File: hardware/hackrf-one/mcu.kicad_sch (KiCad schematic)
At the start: 131 parts, among them J1 USB-MICRO-B, P20 GPIO, P22 I2S, P23 DBGEN, P24 TRST, P25 LPC_ISP, P26 LPC_JTAG, P28 SD, P29 CPLD_JTAG, P3 GND, P30 BANK2_AUX, P5 LEDS, P68 SPIFI_CS, P69 VREGMODE, P70 EN_1V8, P71 ID, P73 P1_2, P74 P1_1, P75 GP_CLKIN, P76 GP_CLKIN, P77 GP_CLKIN, P78 GP_CLKIN, P79 GP_CLKIN, P80 SHIELD, P81 SPIFI_SIO2, P82 SPIFI_SIO3, Q5 MOSFET_P, SW1 DFU, SW2 RESET, U15 TVS, U20 W25Q80, U21 TPS62410, U23 LPC4320FBD144, U24 GSG-XC2C64A-7VQG100C, X2 MCU_XTAL, X3 RTC_XTAL

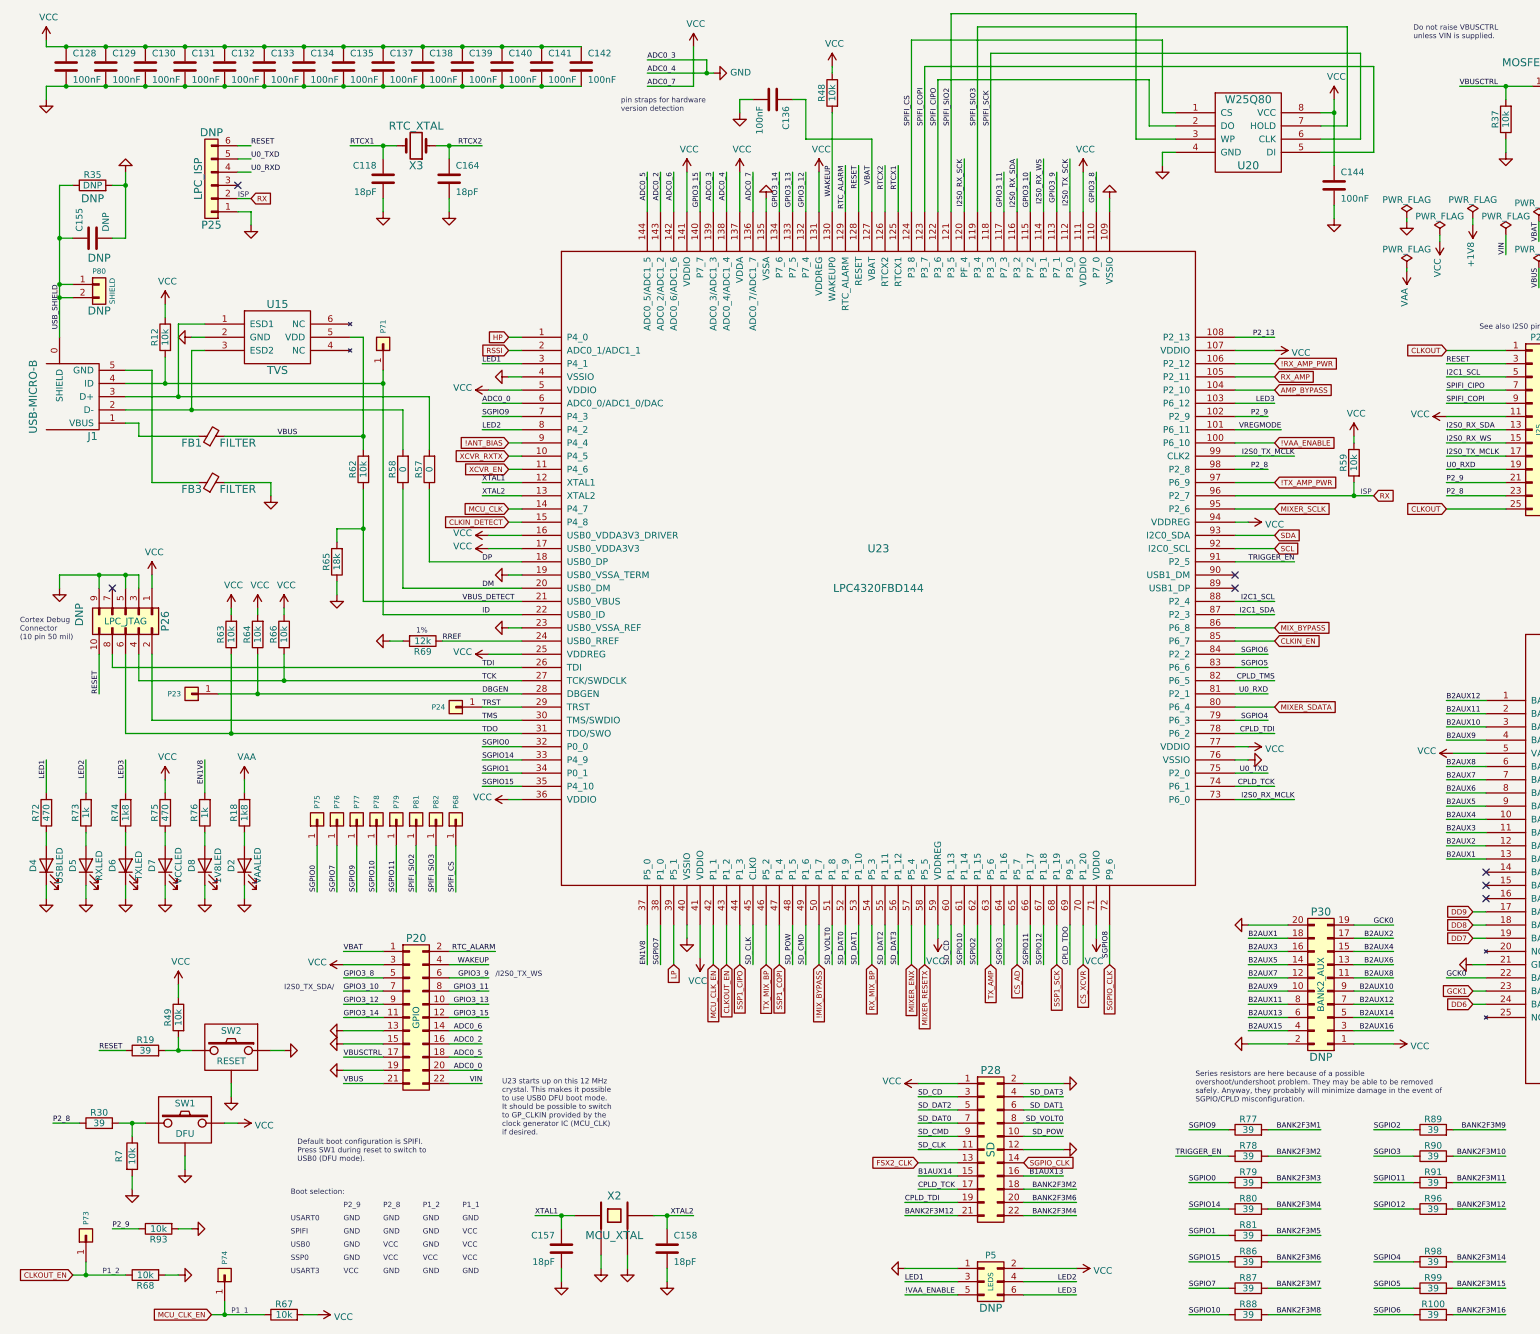
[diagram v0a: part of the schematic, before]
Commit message: HackRF One: revert hardware design to 8727449
This commit is between r8 and r9 and will be used as the basis for r10.
It includes some of the changes in r9 but predates the major changes to
the clock generator and IF transceiver ICs.
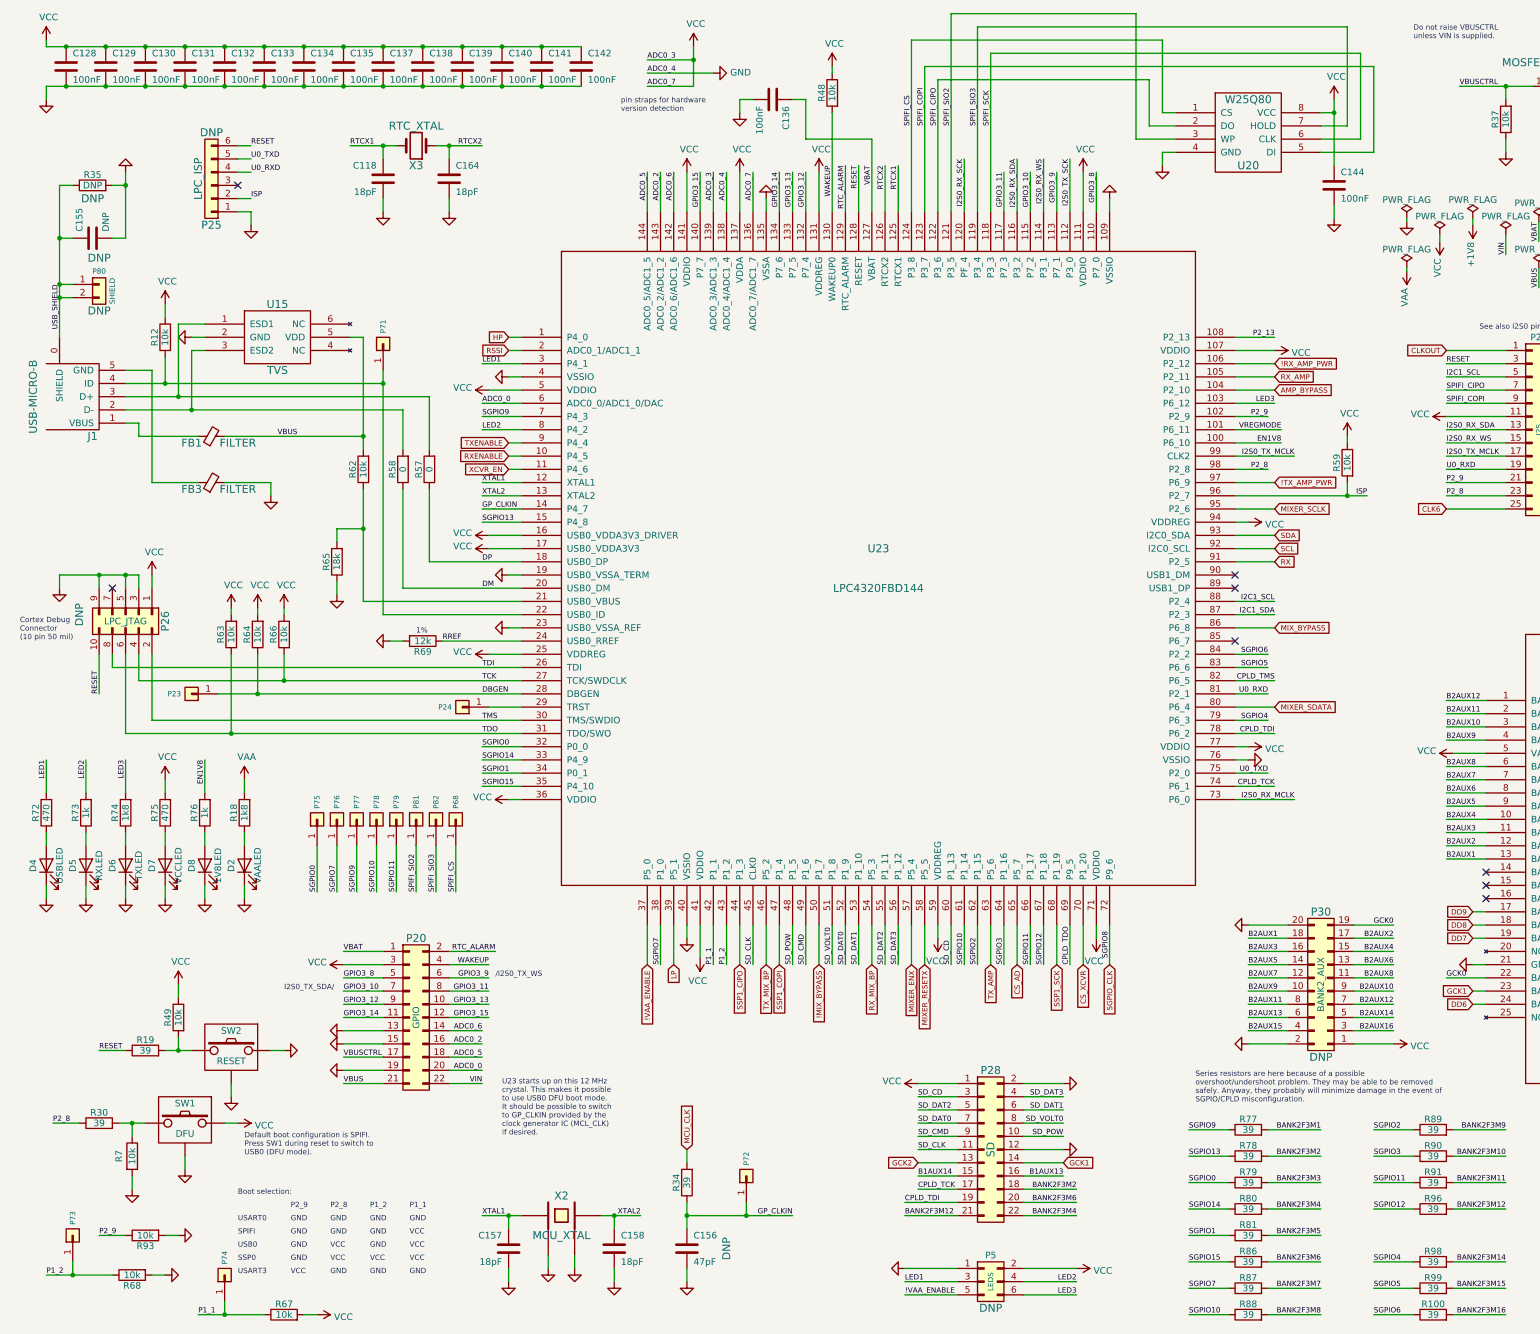
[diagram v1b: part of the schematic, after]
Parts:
- added C156: 47pF, hackrf:GSG-0402, symbol Device:C
- added P72: GP_CLKIN, hackrf:GSG-TESTPOINT-50MIL, symbol Connector_Generic:Conn_01x01
- added R34: 39, hackrf:GSG-0402, symbol Device:R
- C118, C157, C158, C164: Manufacturer Samsung -> Murata; Part Number CL05C180JB5NNNC -> GRM1555C1H180JA01D
- C125: Manufacturer Samsung -> Murata; Part Number CL05C330JB5NNNC -> GRM1555C1H330JA01D
- C126, C127, C143, C145, C146: Manufacturer Samsung -> Murata; Part Number CL21A106KOQNNNE -> GRM21BR61A106KE19L
- C128, C129, C130, C131, C132, C133, C134, C135, C136, C137, C138, C139, C140, C141, C142, C144, C147, C148, C149, C150, C151, C152, C153, C154: Manufacturer Samsung -> Murata; Part Number CL05A104KA5NNNC -> GRM155R61A104KA01D
- C155, NT1, NT2, P23, P24, P25, P26, P29, P3, P30, P5, P68, P69, P70, P71, P73, P74, P75, P76, P77, P78, P79, P80, P81, P82, R35: DNP DNP -> (none); Note (none) -> DNP
- L10, L11: Part Number NRS4018T4R7MDGJ -> NRG4026T4R7M
- Q5: Manufacturer Yangzhou Yangjie -> Alpha and Omega; Part Number YJL2301C -> AO3407A
- R69: Manufacturer Yageo -> Rohm; Part Number RC0402FR-0712KL -> MCR01MRTF1202
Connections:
- net FSX2_CLK is gone; now on net GCK2: P28.13 (Pin_13)
- net !VAA_ENABLE: now also U23.37 (P5_0); no longer U23.100 (P6_10)
- net CLKOUT: no longer P22.25 (Pin_25)
- net EN1V8: now also U23.100 (P6_10); no longer U23.37 (P5_0)
- net GCK1: now also P28.14 (Pin_14)
- net GND: now also C156.2; no longer U23.139 (ADC0_3/ADC1_3)
- net MCU_CLK: now also R34.2; no longer U23.14 (P4_7)
- net RX: now also U23.91 (P2_5); no longer P25.2 (Pin_2), R59.2, U23.96 (P2_7)
- net SGPIO_CLK: no longer P28.14 (Pin_14)
- net VCC: now also U23.139 (ADC0_3/ADC1_3)
- net !ANT_BIAS renamed TXENABLE
- net CLKIN_DETECT renamed SGPIO13
- net SGPIO13: now also R78.1
- net CLKIN_EN: no longer names the net of U23.85 (P6_7)
- net CLKOUT_EN renamed P1_2
- net ID: no longer names the net of J1.4 (ID), P71.1 (Pin_1), R12.2, U23.22 (USB0_ID)
- net MCU_CLK_EN renamed P1_1
- removed net TRIGGER_EN: R78.1, U23.91 (P2_5)
- net TRST: no longer names the net of P24.1 (Pin_1), U23.29 (TRST)
- net VBUS_DETECT: no longer names the net of R62.1, R65.2, U23.21 (USB0_VBUS)
- net XCVR_RXTX renamed RXENABLE
- new net CLK6: P22.25 (Pin_25)
- new net GP_CLKIN: C156.1, P72.1 (Pin_1), R34.1, U23.14 (P4_7)
- new net ISP: P25.2 (Pin_2), R59.2, U23.96 (P2_7)
- no-connect marks 14 -> 15
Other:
- note added: "U23 starts up on this 12 MHz crystal. This makes it possible to use USB0 DFU boot mode. It should be possible to switch to GP_CLKIN provided by the clock generator IC (MCL_CLK) if desired."
- note removed: "ISP"
- note removed: "U23 starts up on this 12 MHz crystal. This makes it possible to use USB0 DFU boot mode. It should be possible to switch to GP_CLKIN provided by the clock generator IC (MCU_CLK) if desired."
- moved on the sheet: C157, C158, P24, P73, R59, R68, R93, X2

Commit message: HackRF One: update version to 8+
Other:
- company: Copyright 2012-2022 Great Scott Gadgets -> ${COPYRIGHT}
- title: HackRF One -> ${TITLE}
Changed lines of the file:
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@@
   (paper "User" 431.8 279.4)
   (title_block
-    (title "HackRF One")
-    (date "2022-08-28")
-    (rev "r9")
-    (company "Copyright 2012-2022 Great Scott Gadgets")
-    (comment 1 "Michael Ossmann")
-    (comment 2 "Licensed under the CERN-OHL-P v2")
+    (title "${TITLE}")
+    (date "${DATE}")
+    (rev "${VERSION}")
+    (company "${COPYRIGHT}")
+    (comment 1 "${LICENSE}")
   )
   (junction (at 34.29 227.33) (diameter 0) (color 0 0 0 0)

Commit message: HackRF One: use DNP field instead of Note field
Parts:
- C155, C156, NT1, NT2, P23, P24, P25, P26, P29, P3, P30, P5, P68, P69, P70, P71, P72, P73, P74, P75, P76, P77, P78, P79, P80, P81, P82, R35: DNP (none) -> DNP; Note DNP -> (none)
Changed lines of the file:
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@@
       (effects (font (size 1.524 1.524)) hide)
     )
-    (property "Note" "DNP" (id 4) (at 49.53 36.83 0)
+    (property "DNP" "DNP" (id 4) (at 49.53 36.83 0)
       (effects (font (size 1.524 1.524)))
     )
@@
       (effects (font (size 1.524 1.524)) hide)
     )
-    (property "Note" "DNP" (id 7) (at 24.13 129.54 0)
+    (property "DNP" "DNP" (id 7) (at 24.13 129.54 0)
       (effects (font (size 1.524 1.524)))
     )
@@
       (effects (font (size 1.524 1.524)) hide)
     )
-    (property "Note" "DNP" (id 4) (at 412.75 232.41 0)
+    (property "DNP" "DNP" (id 4) (at 412.75 232.41 0)
       (effects (font (size 1.524 1.524)))
     )
@@
       (effects (font (size 1.524 1.524)) hide)
     )
-    (property "Note" "DNP" (id 7) (at 148.59 251.46 90)
+    (property "DNP" "DNP" (id 7) (at 148.59 251.46 90)
       (effects (font (size 1.524 1.524)))
     )
@@
       (effects (font (size 1.524 1.524)) hide)
     )
-    (property "Note" "DNP" (id 4) (at 382.27 76.2 0)
+    (property "DNP" "DNP" (id 4) (at 382.27 76.2 0)
       (effects (font (size 1.524 1.524)))
     )
@@
       (effects (font (size 1.524 1.524)) hide)
     )
-    (property "Note" "DNP" (id 4) (at 262.89 214.63 0)
+    (property "DNP" "DNP" (id 4) (at 262.89 214.63 0)
       (effects (font (size 1.524 1.524)))
     )
@@
       (effects (font (size 1.524 1.524)) hide)
     )
-    (property "Note" "DNP" (id 4) (at 45.72 144.78 0)
+    (property "DNP" "DNP" (id 4) (at 45.72 144.78 0)
       (effects (font (size 1.524 1.524)) hide)
     )
@@
       (effects (font (size 1.524 1.524)) hide)
     )
-    (property "Note" "DNP" (id 4) (at 97.79 147.32 0)
+    (property "DNP" "DNP" (id 4) (at 97.79 147.32 0)
       (effects (font (size 1.524 1.524)) hide)
     )
@@
       (effects (font (size 1.524 1.524)))
     )
-    (property "Note" "DNP" (id 4) (at 199.39 262.89 0)
+    (property "DNP" "DNP" (id 4) (at 199.39 262.89 0)
       (effects (font (size 1.524 1.524)))
     )
@@
       (effects (font (size 1.524 1.524)) hide)
     )
-    (property "Note" "DNP" (id 4) (at 27.94 71.12 0)
+    (property "DNP" "DNP" (id 4) (at 27.94 71.12 0)
       (effects (font (size 1.524 1.524)))
     )
@@
       (effects (font (size 1.524 1.524)) hide)
     )
-    (property "Note" "DNP" (id 4) (at 88.9 168.91 0)
+    (property "DNP" "DNP" (id 4) (at 88.9 168.91 0)
       (effects (font (size 1.524 1.524)) hide)
     )
@@
       (effects (font (size 1.524 1.524)) hide)
     )
-    (property "Note" "DNP" (id 4) (at 152.4 237.49 0)
+    (property "DNP" "DNP" (id 4) (at 152.4 237.49 0)
       (effects (font (size 1.524 1.524)) hide)
     )
@@
       (effects (font (size 1.524 1.524)) hide)
     )
-    (property "Note" "DNP" (id 4) (at 92.71 168.91 0)
+    (property "DNP" "DNP" (id 4) (at 92.71 168.91 0)
       (effects (font (size 1.524 1.524)) hide)
     )
@@
       (effects (font (size 1.524 1.524)) hide)
     )
-    (property "Note" "DNP" (id 4) (at 82.55 77.47 0)
+    (property "DNP" "DNP" (id 4) (at 82.55 77.47 0)
       (effects (font (size 1.524 1.524)) hide)
     )
@@
       (effects (font (size 1.524 1.524)) hide)
     )
-    (property "Note" "DNP" (id 4) (at 96.52 168.91 0)
+    (property "DNP" "DNP" (id 4) (at 96.52 168.91 0)
       (effects (font (size 1.524 1.524)) hide)
     )
@@
       (effects (font (size 1.524 1.524)) hide)
     )
-    (property "Note" "DNP" (id 4) (at 331.47 33.02 0)
+    (property "DNP" "DNP" (id 4) (at 331.47 33.02 0)
       (effects (font (size 1.524 1.524)) hide)
     )
@@
       (effects (font (size 1.524 1.524)) hide)
     )
-    (property "Note" "DNP" (id 4) (at 410.21 48.26 0)
+    (property "DNP" "DNP" (id 4) (at 410.21 48.26 0)
       (effects (font (size 1.524 1.524)) hide)
     )
@@
       (effects (font (size 1.524 1.524)) hide)
     )
-    (property "Note" "DNP" (id 4) (at 22.86 248.92 0)
+    (property "DNP" "DNP" (id 4) (at 22.86 248.92 0)
       (effects (font (size 1.524 1.524)) hide)
     )
@@
       (effects (font (size 1.524 1.524)) hide)
     )
-    (property "Note" "DNP" (id 4) (at 52.07 256.54 0)
+    (property "DNP" "DNP" (id 4) (at 52.07 256.54 0)
       (effects (font (size 1.524 1.524)) hide)
     )
@@
       (effects (font (size 1.524 1.524)) hide)
     )
-    (property "Note" "DNP" (id 4) (at 69.85 168.91 0)
+    (property "DNP" "DNP" (id 4) (at 69.85 168.91 0)
       (effects (font (size 1.524 1.524)) hide)
     )
@@
       (effects (font (size 1.524 1.524)) hide)
     )
-    (property "Note" "DNP" (id 4) (at 73.66 168.91 0)
+    (property "DNP" "DNP" (id 4) (at 73.66 168.91 0)
       (effects (font (size 1.524 1.524)) hide)
     )
@@
       (effects (font (size 1.524 1.524)) hide)
     )
-    (property "Note" "DNP" (id 4) (at 77.47 168.91 0)
+    (property "DNP" "DNP" (id 4) (at 77.47 168.91 0)
       (effects (font (size 1.524 1.524)) hide)
     )
@@
       (effects (font (size 1.524 1.524)) hide)
     )
-    (property "Note" "DNP" (id 4) (at 81.28 168.91 0)
+    (property "DNP" "DNP" (id 4) (at 81.28 168.91 0)
       (effects (font (size 1.524 1.524)) hide)
     )
@@
       (effects (font (size 1.524 1.524)) hide)
     )
-    (property "Note" "DNP" (id 4) (at 85.09 168.91 0)
+    (property "DNP" "DNP" (id 4) (at 85.09 168.91 0)
       (effects (font (size 1.524 1.524)) hide)
     )
@@
       (effects (font (size 1.524 1.524)))
     )
-    (property "Note" "DNP" (id 4) (at 26.67 49.53 90)
+    (property "DNP" "DNP" (id 4) (at 26.67 49.53 90)
       (effects (font (size 1.524 1.524)))
     )
@@
       (effects (font (size 1.524 1.524)))
     )
-    (property "Note" "DNP" (id 4) (at 27.94 60.96 90)
+    (property "DNP" "DNP" (id 4) (at 27.94 60.96 90)
       (effects (font (size 1.524 1.524)))
     )
@@
       (effects (font (size 1.27 1.27)) hide)
     )
-    (property "Note" "DNP" (id 4) (at 405.13 68.58 0)
+    (property "DNP" "DNP" (id 4) (at 405.13 68.58 0)
       (effects (font (size 1.27 1.27)) hide)
     )
@@
       (effects (font (size 1.27 1.27)) hide)
     )
-    (property "Note" "DNP" (id 4) (at 405.13 17.78 0)
+    (property "DNP" "DNP" (id 4) (at 405.13 17.78 0)
       (effects (font (size 1.27 1.27)) hide)
     )

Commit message: HackRF One: update component selections
Add Substitution field
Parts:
- C118, C157, C158, C164: Manufacturer Murata -> Samsung; Part Number GRM1555C1H180JA01D -> CL05C180JB5NNNC; Substitution (none) -> Murata GRM1555C1H180JA01D
- C125: Manufacturer Murata -> Samsung; Part Number GRM1555C1H330JA01D -> CL05C330JB5NNNC; Substitution (none) -> Murata GRM1555C1H330JA01D
- C126, C127, C143, C145, C146: Manufacturer Murata -> Samsung; Part Number GRM21BR61A106KE19L -> CL21A106KOQNNNE; Substitution (none) -> Murata GRM21BR61A106KE19L
- C156: Manufacturer Murata -> Samsung; Part Number GRM1555C1H470JA01D -> CL05C470JB5NNNC; Substitution (none) -> Murata GRM1555C1H470JA01D
- L10, L11: Part Number NRG4026T4R7M -> NRS4018T4R7MDGJ; Substitution (none) -> NRG4026T4R7M
- Q5: Manufacturer Alpha and Omega -> Yangzhou Yangjie; Part Number AO3407A -> YJL2301C
- R100, R12, R18, R19, R30, R34, R37, R46, R47, R48, R49, R51, R52, R54, R55, R56, R57, R58, R59, R62, R63, R64, R65, R66, R67, R68, R7, R72, R73, R74, R75, R76, R77, R78, R79, R80, R81, R86, R87, R88, R89, R90, R91, R93, R96, R98, R99: Substitution (none) -> any equivalent
- R69: Manufacturer Rohm -> Yageo; Part Number MCR01MRTF1202 -> RC0402FR-0712KL; Substitution (none) -> any equivalent

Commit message: HackRF One: update 100 nF capacitor part selection
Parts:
- C128, C129, C130, C131, C132, C133, C134, C135, C136, C137, C138, C139, C140, C141, C142, C144, C147, C148, C149, C150, C151, C152, C153, C154: Manufacturer Murata -> Samsung; Part Number GRM155R61A104KA01D -> CL05A104KA5NNNC; Substitution (none) -> Murata GRM155R61A104KA01D
